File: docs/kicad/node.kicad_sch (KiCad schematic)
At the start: 9 parts, among them U1 ESP32-DevKitC, U2 ESP32-DevKitC, U3 ESP32-DevKitC, U4 ESP32-DevKitC

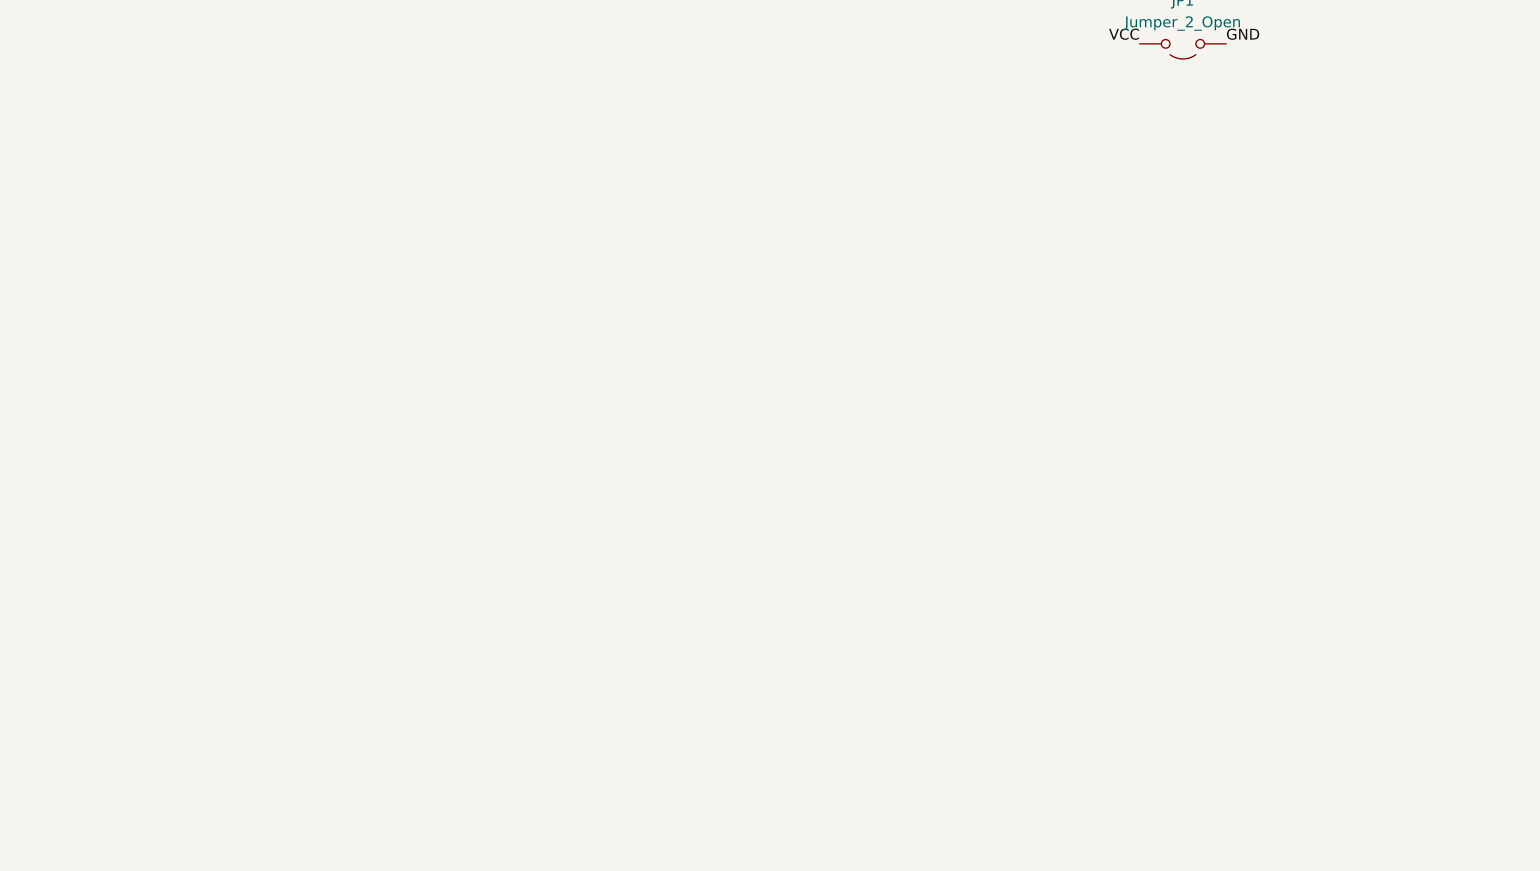
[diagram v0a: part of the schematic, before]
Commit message: Docs: update kicad
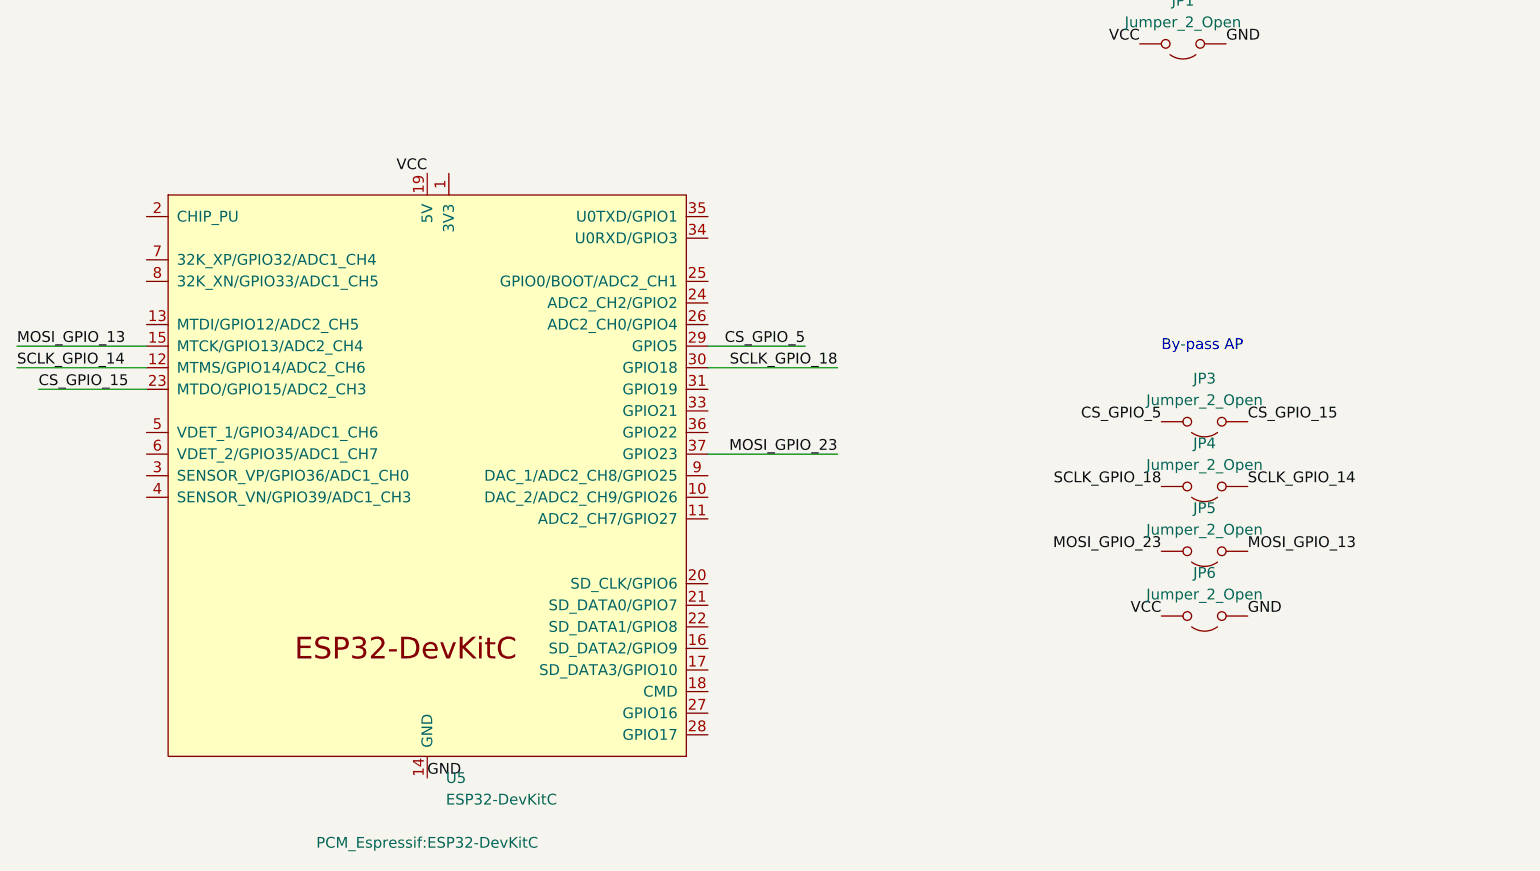
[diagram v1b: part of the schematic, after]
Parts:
- added JP3, JP4, JP5, JP6: Jumper_2_Open, Connector_PinSocket_1.00mm:PinSocket_1x02_P1.00mm_Vertical, symbol Jumper:Jumper_2_Open
- added U5: ESP32-DevKitC, PCM_Espressif:ESP32-DevKitC, symbol PCM_Espressif:ESP32-DevKitC
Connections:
- net GND: now also JP6.1 (A), U5.14 (GND), U5.32 (GND), U5.38 (GND)
- net VCC: now also JP6.2 (B), U5.19 (5V)
- new net CS_GPIO_15: JP3.1 (A), U5.23 (MTDO/GPIO15/ADC2_CH3)
- new net CS_GPIO_5: JP3.2 (B), U5.29 (GPIO5)
- new net MOSI_GPIO_13: JP5.1 (A), U5.15 (MTCK/GPIO13/ADC2_CH4)
- new net MOSI_GPIO_23: JP5.2 (B), U5.37 (GPIO23)
- new net SCLK_GPIO_14: JP4.1 (A), U5.12 (MTMS/GPIO14/ADC2_CH6)
- new net SCLK_GPIO_18: JP4.2 (B), U5.30 (GPIO18)
